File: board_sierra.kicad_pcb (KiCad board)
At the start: 6 copper layers, 90.2 x 95.9 mm, 247 parts, among them M1 S25FL256L, M2 S25FL256L, M3 S25FL256L, M4 CY15B102Q, M5 CY15B102Q, M6 CY15B102Q, Q1 TPS22965-Q1, Q2 TPS22965-Q1, Q3 TPS22965-Q1, U1 STM32L496ZGTx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

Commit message: sync with library
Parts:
- D4: footprint VST104_footprints:D_SMD_SOD523_1.2x0.8mm -> VST104_footprints:D_SOD-523_1.2x0.8mm
- ESD1: footprint VST104_footprints:µDFN-14_3.5x1.35mm -> VST104_footprints:uDFN-14_3.5x1.35mm
- H1, H2: footprint VST104_footprints:ESQ-129-39-x-D -> VST104_footprints:ESQ-126-39-x-D
- UA1, UA2, UA3, UA4: value PC104_SO-24_universal -> Val**

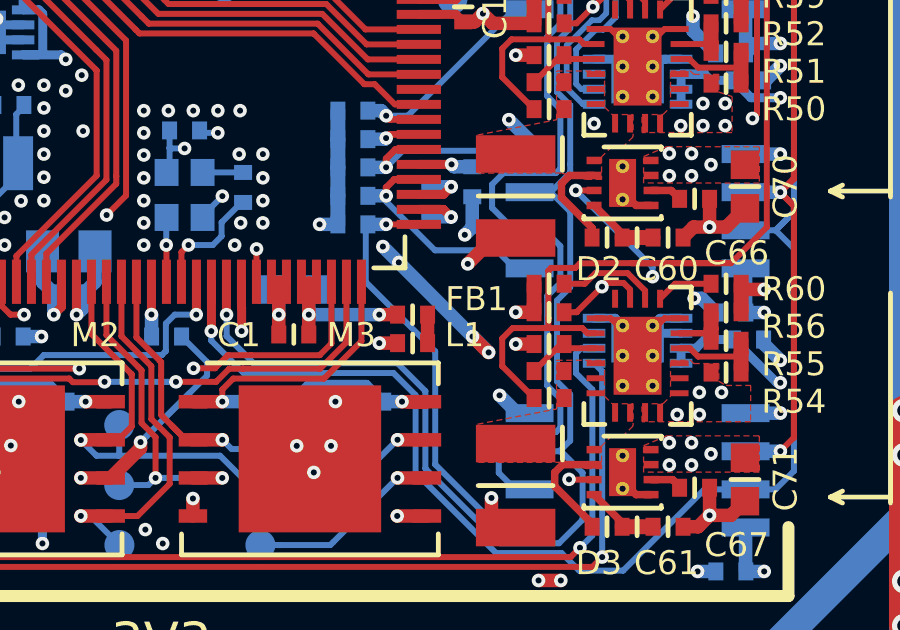
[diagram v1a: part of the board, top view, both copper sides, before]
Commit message: L1 to 0603
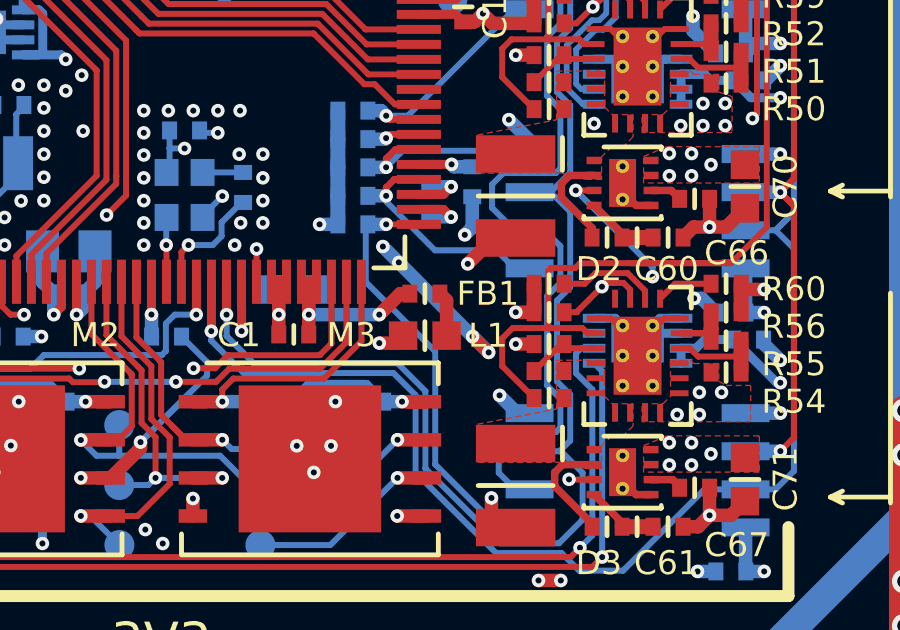
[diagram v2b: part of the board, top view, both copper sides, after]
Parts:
- L1: footprint VST104_footprints:L_SMD_0402 -> VST104_footprints:L_SMD_0603
- UA1, UA2, UA3, UA4: value Val** -> PC104_SO-24_universal
- moved FB1 0.81 mm to (53.4, 70.6)
- moved L1 0.48 mm to (53.4, 72.0)
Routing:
- net +3.3VADC: track 7.76 -> 8.46 mm
- net Net-(FB1-Pad1): track 0.95 -> 1.49 mm
